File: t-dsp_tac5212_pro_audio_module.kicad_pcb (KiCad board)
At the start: 4 copper layers, 42 x 26.5 mm, 110 parts, among them T108 Tab, T109 Tab, T110 Tab, T111 Tab, U108 Single Buffer with Tri-state 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, U109 3.3v LDO - TLV74133PDBVR

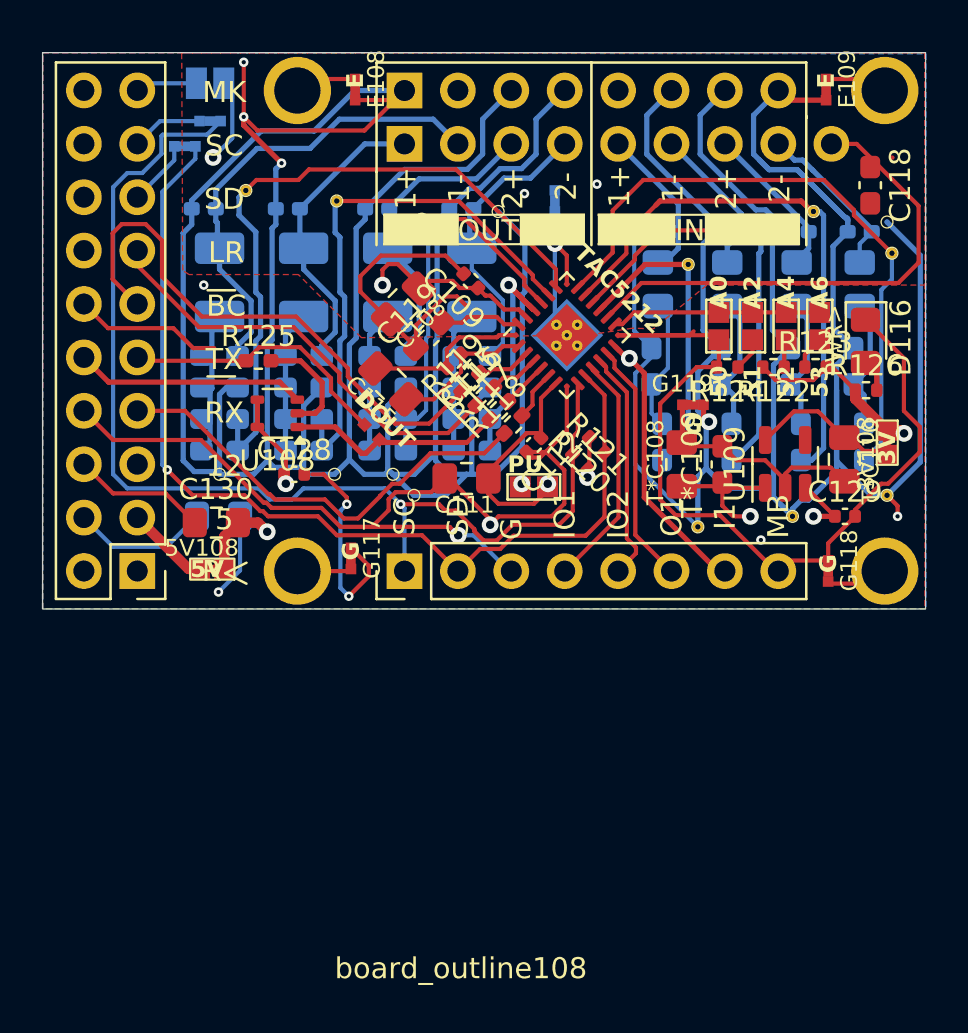
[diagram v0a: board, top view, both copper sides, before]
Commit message: fix all drc errors.
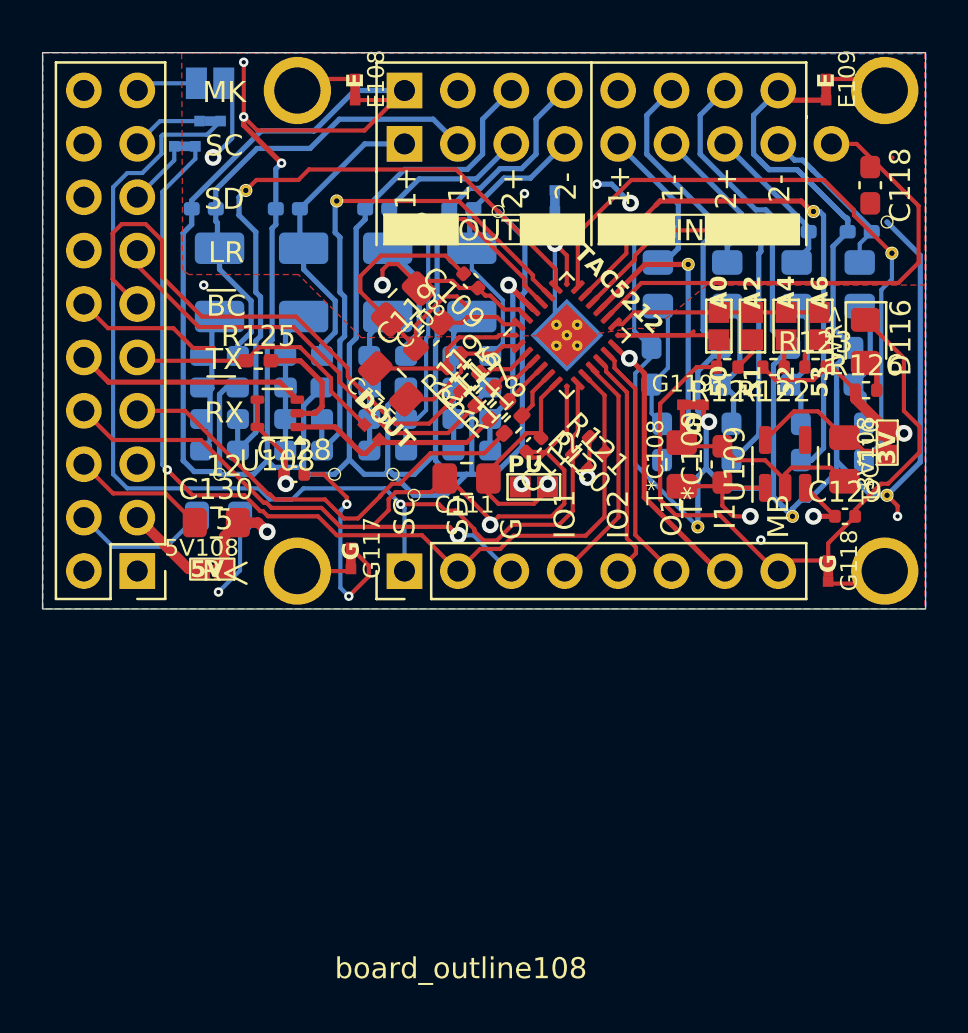
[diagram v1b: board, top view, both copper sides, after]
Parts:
- FB108, FB109, FB110, FB111: footprint project_fp:C_0805_2012Metric_Pad1.18x1.45mm_HandSolder -> project_fp:L_0805_2012Metric_Pad1.18x1.45mm_HandSolder
- R108, R109, R111, R116, R127, R129, R130, R131, R132, R133, R134, R135, R136, R137, R138, R139: footprint Capacitor_SMD:C_0603_1608Metric_Pad1.08x0.95mm_HandSolder -> project_fp:R_0603_1608Metric_Pad1.05x0.95mm_HandSolder
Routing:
- net Earth: track 295.5 -> 297.5 mm, vias 8 -> 9
- net IN1M: track 21.4 -> 20.9 mm

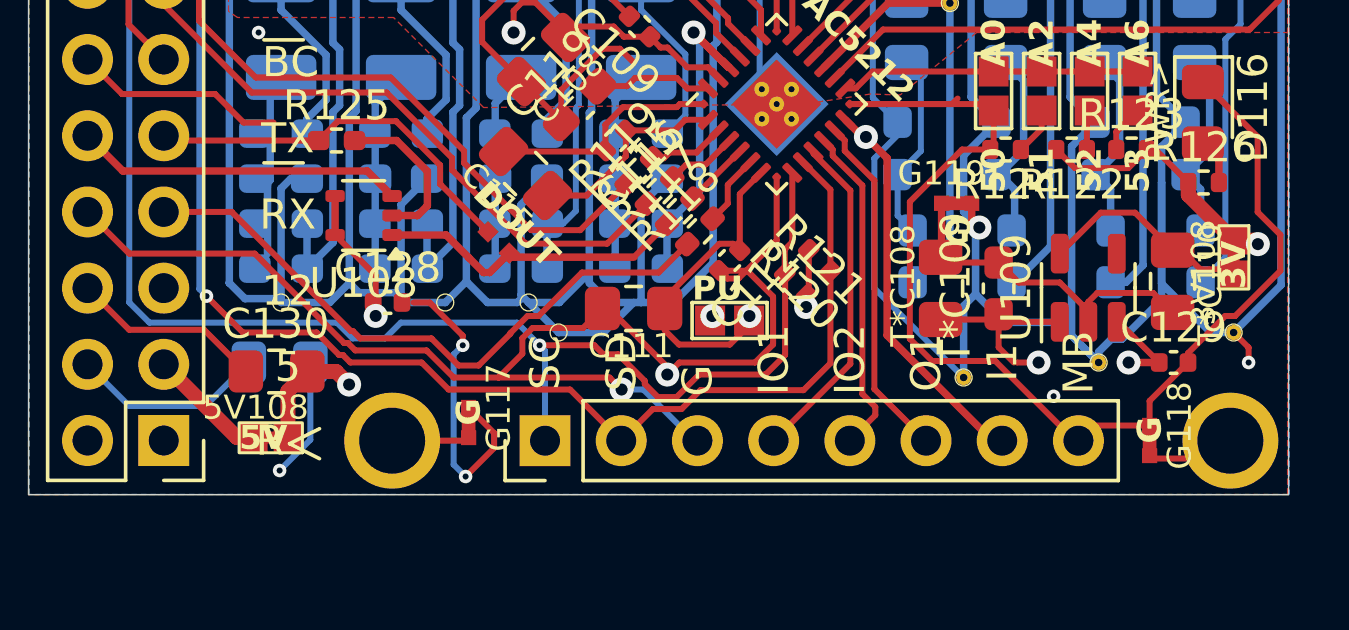
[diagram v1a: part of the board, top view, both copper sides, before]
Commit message: Add KiBot CI/CD pipeline for JLCPCB manufacturing files
- Add .kibot.yaml config for gerbers, drill, BOM, CPL, and ZIP output
- Add GitHub Actions workflow triggered on push to main and manual dispatch
- Add release job to attach JLCPCB ZIP to GitHub Releases on version tags
- Fix malformed reference designators (5V108, 3V108) that blocked KiBot BOM/CPL
- Add local build instructions to README
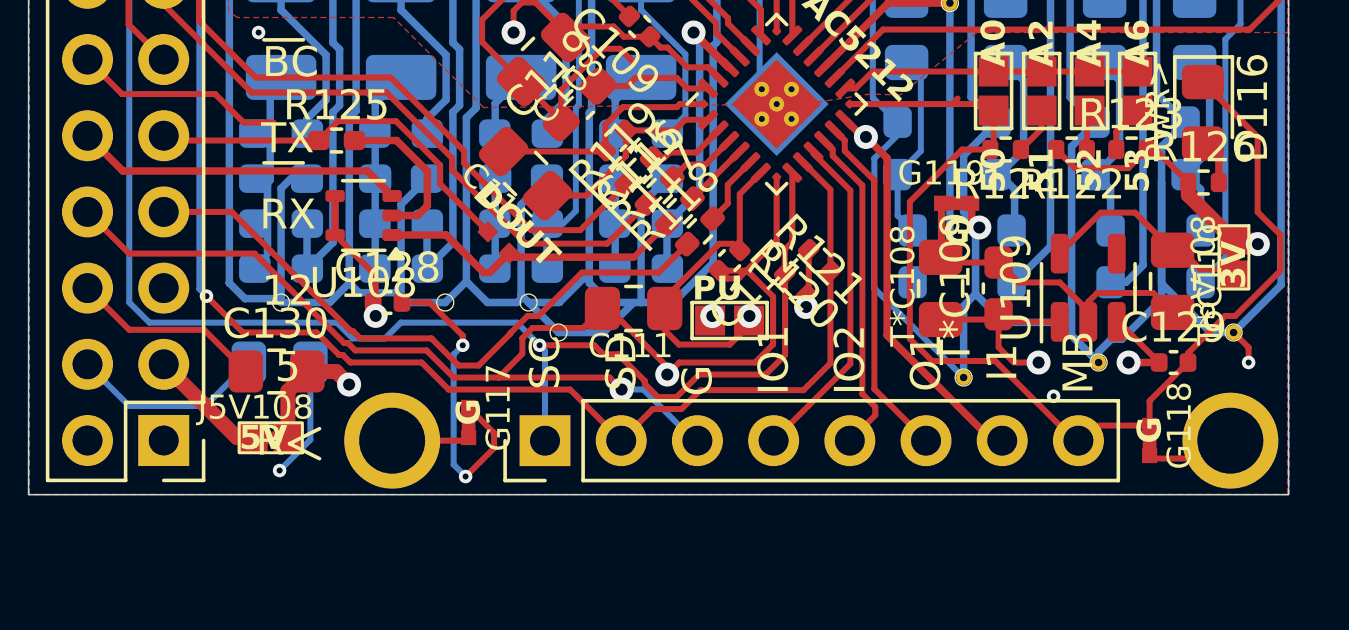
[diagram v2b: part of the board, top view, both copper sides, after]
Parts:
- renumbered 3V108 to J3V108, 5V108 to J5V108
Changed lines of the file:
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@@
 	(net 68 "Net-(TAC5212-DIN)")
 	(net 69 "Net-(TAC5212-BCLK)")
-	(net 70 "Net-(5V108-Pad2)")
+	(net 70 "Net-(J5V108-Pad2)")
 	(footprint "project_fp:R_0402_1005Metric"
 		(layer "F.Cu")
@@
 			(layers "*.Cu" "*.Mask")
 			(remove_unused_layers no)
-			(net 70 "Net-(5V108-Pad2)")
+			(net 70 "Net-(J5V108-Pad2)")
 			(pinfunction "5V")
 			(pintype "passive")
@@
 		(descr "net tie")
 		(tags "net tie")
-		(property "Reference" "3V108"
+		(property "Reference" "J3V108"
 			(at 0.5 1 90)
 			(layer "F.SilkS")
@@
 			)
 		)
-		(property ki_fp_filters "SOT?23*")
+		(property ki_fp_filters "SOT?23* SC?70* SOT-353*")
 		(sheetname "/")
 		(sheetfile "t-dsp_tac5212_pro_audio_module.kicad_sch")
@@
 			)
 		)
-		(property ki_fp_filters "Connector*:*_2x??_*")
+		(property ki_fp_filters "VQFN*")
 		(sheetname "/")
 		(sheetfile "t-dsp_tac5212_pro_audio_module.kicad_sch")
@@
 		(descr "net tie")
 		(tags "net tie")
-		(property "Reference" "5V108"
+		(property "Reference" "J5V108"
 			(at 0.5 1 180)
 			(layer "F.SilkS")
@@
 			(size 0.954 1)
 			(layers "F.Cu")
-			(net 70 "Net-(5V108-Pad2)")
+			(net 70 "Net-(J5V108-Pad2)")
 			(pinfunction "2")
 			(pintype "passive")
